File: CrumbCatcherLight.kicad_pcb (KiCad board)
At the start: 2 copper layers, 60.1 x 69.1 mm, 57 parts, among them J1 USB_C_Receptacle, J2 Conn_01x03, J3 Conn_ARM_SWD_TagConnect_TC203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, SW10 SW_SPST, SW11 EVPAA202K, SW2 PEC11R, SW3 SW_SPST, SW4 SW_SPST, SW5 PEC11R, SW6 SW_SPST, SW7 SW_SPST, SW8 PEC11R, SW9 SW_SPST, U0 PCB, U1 ECMF02-2AMX6, U2 MDBT50Q-U1MV2, U6 BQ24075RGT

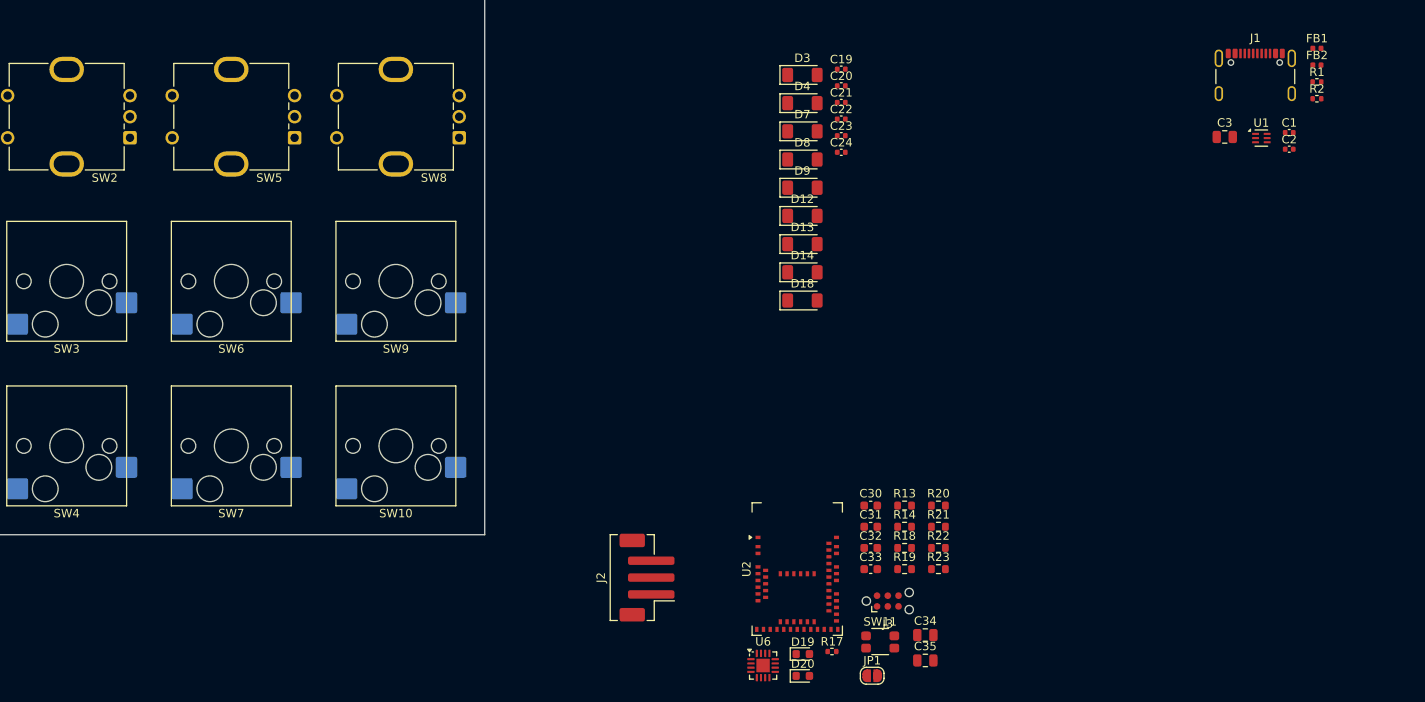
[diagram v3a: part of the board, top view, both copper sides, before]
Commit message: Add some todo notes, add 3/2 pin battery connectors
Add NTC connector, Update power scheme for RF module
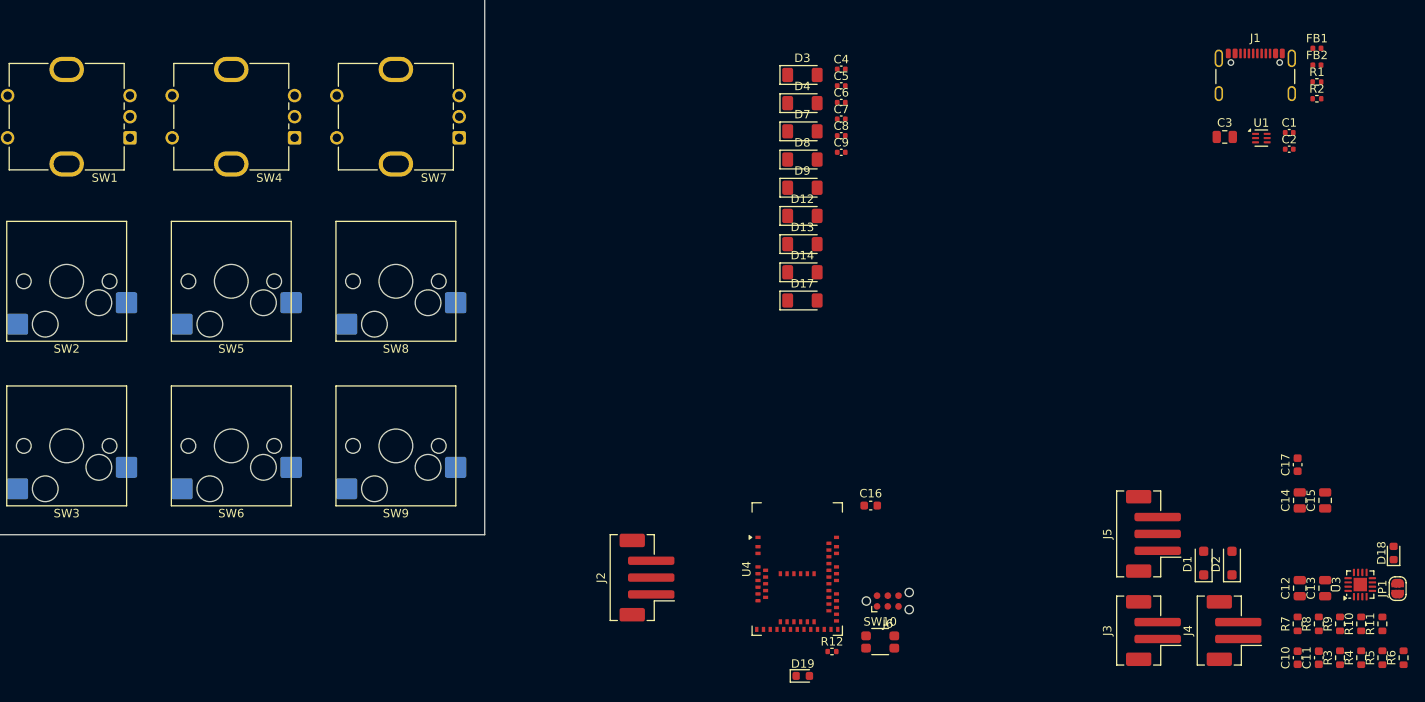
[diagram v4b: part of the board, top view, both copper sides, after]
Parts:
- removed C31: 8pF, Capacitor_SMD:C_0603_1608Metric
- removed C32: 1uF, Capacitor_SMD:C_0603_1608Metric
- removed C33: 100nF, Capacitor_SMD:C_0603_1608Metric
- removed C34, C35: 4.7uF, Capacitor_SMD:C_0805_2012Metric
- removed the D19 at (198.2, 155.2)
- removed R13: 2M, Resistor_SMD:R_0603_1608Metric
- removed R14: 806k, Resistor_SMD:R_0603_1608Metric
- removed R18, R19, R23: 1K, Resistor_SMD:R_0603_1608Metric
- removed R20, R21, R22: 10K, Resistor_SMD:R_0603_1608Metric
- removed U6: BQ24075RGT, Package_DFN_QFN:VQFN-16-1EP_3x3mm_P0.5mm_EP1.6x1.6mm
- added C10: 1uF, Capacitor_SMD:C_0603_1608Metric, F.Cu at (256.8, 155.6)
- added C11: 100nF, Capacitor_SMD:C_0603_1608Metric, F.Cu at (259.3, 155.6)
- added C12: 4.7uF, Capacitor_SMD:C_0805_2012Metric, F.Cu at (257.1, 147.4)
- added C13: 4.7uF, Capacitor_SMD:C_0805_2012Metric, F.Cu at (260.1, 147.4)
- added C14: 10uF, Capacitor_SMD:C_0805_2012Metric, F.Cu at (257.1, 137.0)
- added C15: 10uF, Capacitor_SMD:C_0805_2012Metric, F.Cu at (260.1, 137.0)
- added C17: 12pF, Capacitor_SMD:C_0603_1608Metric, F.Cu at (256.8, 132.7)
- added D1: MBR1020VL, Diode_SMD:D_SOD-123F, F.Cu at (245.7, 144.4)
- added D18: Yellow, LED_SMD:LED_0603_1608Metric, F.Cu at (268.2, 143.2)
- added D2: MBR1020VL, Diode_SMD:D_SOD-123F, F.Cu at (249.1, 144.4)
- added J3: Battery No NTC, Connector_JST:JST_PH_B2B-PH-SM4-TB_1x02-1MP_P2.00mm_Vertical, F.Cu at (239.8, 152.4)
- added J4: NTC, Connector_JST:JST_PH_B2B-PH-SM4-TB_1x02-1MP_P2.00mm_Vertical, F.Cu at (249.3, 152.4)
- added J5: Qi Charger In, Connector_JST:JST_PH_B3B-PH-SM4-TB_1x03-1MP_P2.00mm_Vertical, F.Cu at (239.8, 140.9)
- added R10: 2M, Resistor_SMD:R_0603_1608Metric, F.Cu at (264.4, 151.6)
- added R11: 10K, Resistor_SMD:R_0603_1608Metric, F.Cu at (266.9, 151.6)
- added R3: 1K, Resistor_SMD:R_0603_1608Metric, F.Cu at (261.9, 155.6)
- added R4: 1K, Resistor_SMD:R_0603_1608Metric, F.Cu at (264.4, 155.6)
- added R5: 1K, Resistor_SMD:R_0603_1608Metric, F.Cu at (266.9, 155.6)
- added R6: 1K, Resistor_SMD:R_0603_1608Metric, F.Cu at (269.4, 155.6)
- added R7: 10K, Resistor_SMD:R_0603_1608Metric, F.Cu at (256.8, 151.6)
- added R8: 10K, Resistor_SMD:R_0603_1608Metric, F.Cu at (259.3, 151.6)
- added R9: 806k, Resistor_SMD:R_0603_1608Metric, F.Cu at (261.9, 151.6)
- added U3: BQ24075RGT, Package_DFN_QFN:VQFN-16-1EP_3x3mm_P0.5mm_EP1.6x1.6mm, F.Cu at (264.2, 146.9)
- C16: renamed from C30; value 8pF -> 12pF
- J2: value Conn_01x03 -> Battery with NTC
- moved JP1 63.1 mm to (268.7, 147.4), turned to 90 degrees
- renumbered C19 to C4, C20 to C5, C21 to C6, C22 to C7, C23 to C8, C24 to C9, D18 to D17, D20 to D19, J3 to J6, R17 to R12, SW2 to SW1, SW11 to SW10, SW3 to SW2, SW4 to SW3, SW5 to SW4, SW6 to SW5, SW7 to SW6, SW8 to SW7, SW9 to SW8, SW10 to SW9, U0 to U2, U2 to U4
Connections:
- FB1 pad 2: +5V -> Net-(D1-A)
- J2 pad 1: GND -> +VBATT
- J2 pad 2: /nRF52840/VBAT -> /BATT_TS
- J2 pad MP: (no net) -> GND
- U4 pad 28: /nRF52840/VDDH -> Net-(U4-VDD)
- U4 pad 30: /nRF52840/VDDH -> +5V
- U4 pad 31: unconnected-(U2-DCCH-Pad31) -> Net-(U4-DCCH)

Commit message: Update BOM
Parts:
- removed C13: 4.7uF, Capacitor_SMD:C_0805_2012Metric
- removed C9: 100nF, Capacitor_SMD:C_0402_1005Metric
- removed R12: 1K, Resistor_SMD:R_0402_1005Metric
- added C18: 10uF, Capacitor_SMD:C_0805_2012Metric, F.Cu at (238.0, 53.0)
- added C19: 10uF, Capacitor_SMD:C_0805_2012Metric, F.Cu at (241.4, 62.5)
- added L1: 10uH, Inductor_SMD:L_0603_1608Metric, F.Cu at (233.7, 55.2)
- added R13: 1K, Resistor_SMD:R_0603_1608Metric, F.Cu at (233.7, 57.7)
- added X1: 32.768kHz, Mad_Footprints:XTAL_FC-12M, F.Cu at (237.6, 56.0)
- C1, C2, C4, C5, C6, C7, C8: footprint Capacitor_SMD:C_0402_1005Metric -> Capacitor_SMD:C_0603_1608Metric
- C12: value 4.7uF -> 100nF; footprint Capacitor_SMD:C_0805_2012Metric -> Capacitor_SMD:C_0603_1608Metric
- D1, D2: value MBR1020VL -> MBR120VL
- moved C12 87.2 mm to (227.7, 65.3), turned to 0 degrees
- moved C17 83.3 mm to (233.7, 52.7), turned to 0 degrees
- moved D1 82.5 mm to (234.5, 62.7), turned to 0 degrees
- moved C4 41.5 mm to (227.7, 52.7)
- moved C5 41.1 mm to (227.7, 55.2)
- moved C6 40.6 mm to (227.7, 57.7)
- moved C7 40.2 mm to (227.7, 60.2)
- moved C8 39.8 mm to (227.7, 62.8)
- moved C1 35.5 mm to (233.7, 65.6)
- moved C2 35.1 mm to (233.7, 68.1)
- renumbered U2 to U0
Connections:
- net /Battery Charger/BVOLT renamed /BVOLT
- C12 pad 1: /Battery Charger/VDDH -> /Switches/ENC3A
- C14 pad 2: +5V -> VDDH
- C4 pad 1: /Switches/ENC1A -> GND
- C4 pad 2: GND -> /Switches/ENC1B
- C5 pad 1: GND -> /Switches/ENC1A
- C5 pad 2: /Switches/ENC1B -> GND
- C6 pad 1: /Switches/ENC2A -> GND
- C6 pad 2: GND -> /Switches/ENC2B
- C7 pad 1: GND -> /Switches/ENC2A
- C7 pad 2: /Switches/ENC2B -> GND
- C8 pad 1: /Switches/ENC3A -> GND
- C8 pad 2: GND -> /Switches/ENC3B
- R8 pad 1: /Battery Charger/VDDH -> VDDH
- U3 pad 10: /Battery Charger/VDDH -> VDDH
- U3 pad 11: /Battery Charger/VDDH -> VDDH
- U3 pad 6: /Battery Charger/VDDH -> VDDH
- U4 pad 30: +5V -> VDDH

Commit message: Add some research, update switches
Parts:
- removed C12: 100nF, Capacitor_SMD:C_0603_1608Metric
- removed the C4 at (227.7, 52.7)
- removed the C5 at (227.7, 55.2)
- removed the C6 at (227.7, 57.7)
- removed the C7 at (227.7, 60.2)
- removed the C8 at (227.7, 62.8)
- removed D12, D13, D14, D17, D7, D8, D9: LL4148, Diode_SMD:D_MiniMELF
- removed the D3 at (198.2, 86.6)
- removed the D4 at (198.2, 89.9)
- added D39: SK6812_MINI_E, Mad_Footprints:SK6812MINI-E, F.Cu at (248.0, 21.1)
- added D40: SK6812_MINI_E, Mad_Footprints:SK6812MINI-E, F.Cu at (248.0, 26.9)
- added D41: SK6812_MINI_E, Mad_Footprints:SK6812MINI-E, F.Cu at (248.0, 32.8)
- added D42: SK6812_MINI_E, Mad_Footprints:SK6812MINI-E, F.Cu at (248.0, 38.5)
- added D43: SK6812MINI, Mad_Footprints:SK6812MINI-012, F.Cu at (241.1, 20.8)
- added D44: SK6812MINI, Mad_Footprints:SK6812MINI-012, F.Cu at (241.1, 25.8)
- added D45: SK6812_MINI_E, Mad_Footprints:SK6812MINI-E, F.Cu at (256.1, 21.1)
- added D46: SK6812_MINI_E, Mad_Footprints:SK6812MINI-E, F.Cu at (256.1, 26.9)
- added D47: SK6812_MINI_E, Mad_Footprints:SK6812MINI-E, F.Cu at (256.1, 32.8)
- added D48: SK6812_MINI_E, Mad_Footprints:SK6812MINI-E, F.Cu at (256.1, 38.5)
- added D49: SK6812MINI, Mad_Footprints:SK6812MINI-012, F.Cu at (241.1, 30.9)
- added D50: SK6812_MINI_E, Mad_Footprints:SK6812MINI-E, F.Cu at (264.1, 21.1)
- added D51: SK6812_MINI_E, Mad_Footprints:SK6812MINI-E, F.Cu at (264.1, 26.9)
- added D52: SK6812_MINI_E, Mad_Footprints:SK6812MINI-E, F.Cu at (264.1, 32.8)
- added D53: SK6812_MINI_E, Mad_Footprints:SK6812MINI-E, F.Cu at (264.1, 38.5)
- added D54: SK6812MINI, Mad_Footprints:SK6812MINI-012, F.Cu at (241.1, 35.9)
- added D55: SK6812MINI, Mad_Footprints:SK6812MINI-012, F.Cu at (241.1, 41.0)
- added D56: SK6812_MINI_E, Mad_Footprints:SK6812MINI-E, F.Cu at (272.1, 21.1)
- added D57: SK6812_MINI_E, Mad_Footprints:SK6812MINI-E, F.Cu at (272.1, 26.9)
- added D58: SK6812_MINI_E, Mad_Footprints:SK6812MINI-E, F.Cu at (272.1, 32.8)
- added D59: SK6812_MINI_E, Mad_Footprints:SK6812MINI-E, F.Cu at (272.1, 38.5)
- added SW10: SW_SPST, kbd:keyswitch_choc12_hotswap_1u, F.Cu at (-59.2, 39.8)
- added SW11: SW_SPST, kbd:keyswitch_choc12_hotswap_1u, F.Cu at (-59.2, 56.0)
- added SW12: SW_SPST, kbd:keyswitch_choc12_hotswap_1u, F.Cu at (-59.2, 72.3)
- added SW13: SW_SPST, kbd:keyswitch_choc12_hotswap_1u, F.Cu at (-59.2, 88.5)
- added SW14: SW_SPST, kbd:keyswitch_choc12_hotswap_1u, F.Cu at (-59.2, 104.8)
- added SW15: SW_SPST, kbd:keyswitch_choc12_hotswap_1u, F.Cu at (-59.2, 121.0)
- added SW16: SW_SPST, kbd:keyswitch_choc12_hotswap_1u, F.Cu at (-41.9, 23.6)
- added SW17: SW_SPST, kbd:keyswitch_choc12_hotswap_1u, F.Cu at (-41.9, 39.8)
- added SW18: SW_SPST, kbd:keyswitch_choc12_hotswap_1u, F.Cu at (-41.9, 56.0)
- added SW19: SW_SPST, kbd:keyswitch_choc12_hotswap_1u, F.Cu at (-41.9, 72.3)
- added SW2: SW_SPST, kbd:keyswitch_choc12_hotswap_1u, F.Cu at (-76.5, 23.6)
- added SW20: SW_SPST, kbd:keyswitch_choc12_hotswap_1u, F.Cu at (-41.9, 88.5)
- added SW21: SW_SPST, kbd:keyswitch_choc12_hotswap_1u, F.Cu at (-41.9, 104.8)
- added SW22: SW_SPST, kbd:keyswitch_choc12_hotswap_1u, F.Cu at (-41.9, 121.0)
- added SW23: SW_SPST, kbd:keyswitch_choc12_hotswap_1u, F.Cu at (-24.6, 23.6)
- added SW24: SW_SPST, kbd:keyswitch_choc12_hotswap_1u, F.Cu at (-24.6, 39.8)
- added SW25: SW_SPST, kbd:keyswitch_choc12_hotswap_1u, F.Cu at (-24.6, 56.0)
- added SW26: SW_SPST, kbd:keyswitch_choc12_hotswap_1u, F.Cu at (-24.6, 72.3)
- added SW27: SW_SPST, kbd:keyswitch_choc12_hotswap_1u, F.Cu at (-24.6, 88.5)
- added SW28: SW_SPST, kbd:keyswitch_choc12_hotswap_1u, F.Cu at (-24.6, 104.8)
- added SW29: SW_SPST, kbd:keyswitch_choc12_hotswap_1u, F.Cu at (-24.6, 121.0)
- added SW3: SW_SPST, kbd:keyswitch_choc12_hotswap_1u, F.Cu at (-76.5, 39.8)
- added SW30: SW_SPST, kbd:keyswitch_choc12_hotswap_1u, F.Cu at (-7.30, 23.6)
- added SW31: SW_SPST, kbd:keyswitch_choc12_hotswap_1u, F.Cu at (-7.30, 39.8)
- added SW32: SW_SPST, kbd:keyswitch_choc12_hotswap_1u, F.Cu at (-7.30, 56.0)
- added SW33: SW_SPST, kbd:keyswitch_choc12_hotswap_1u, F.Cu at (-7.30, 72.3)
- added SW34: SW_SPST, kbd:keyswitch_choc12_hotswap_1u, F.Cu at (-7.30, 88.5)
- added SW35: SW_SPST, kbd:keyswitch_choc12_hotswap_1u, F.Cu at (-7.30, 104.8)
- added SW4: SW_SPST, kbd:keyswitch_choc12_hotswap_1u, F.Cu at (-76.5, 56.0)
- added SW5: SW_SPST, kbd:keyswitch_choc12_hotswap_1u, F.Cu at (-76.5, 72.3)
- added SW6: SW_SPST, kbd:keyswitch_choc12_hotswap_1u, F.Cu at (-76.5, 88.5)
- added SW7: SW_SPST, kbd:keyswitch_choc12_hotswap_1u, F.Cu at (-76.5, 104.8)
- added SW8: SW_SPST, kbd:keyswitch_choc12_hotswap_1u, F.Cu at (-76.5, 121.0)
- added SW9: SW_SPST, kbd:keyswitch_choc12_hotswap_1u, F.Cu at (-59.2, 23.6)
- renumbered C16 to C10, C17 to C11, C10 to C4, C11 to C5, C19 to C6, C14 to C7, C18 to C8, C15 to C9, D2 to D1, D1 to D2, D18 to D3, D19 to D4, J5 to J2, J2 to J3, J3 to J4, J4 to J5, R13 to R12, SW10 to SW1, U0 to U2
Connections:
- D1 pad 2: Net-(D2-A) (its old number) -> +5V
- D3 pad 2: Net-(D18-A) -> Net-(D3-A)
- D4 pad 2: Net-(D19-A) -> Net-(D4-A)
- J2 pad 1: Net-(D2-A) (its old number) -> +5V
- R12 pad 1: Net-(D19-A) -> Net-(D4-A)
- R8 pad 2: Net-(D18-A) -> Net-(D3-A)
